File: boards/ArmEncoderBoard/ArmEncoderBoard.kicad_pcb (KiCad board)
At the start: 2 copper layers, 34 x 42.5 mm, 5 parts, among them J1 S6B-PH-SM4-TB

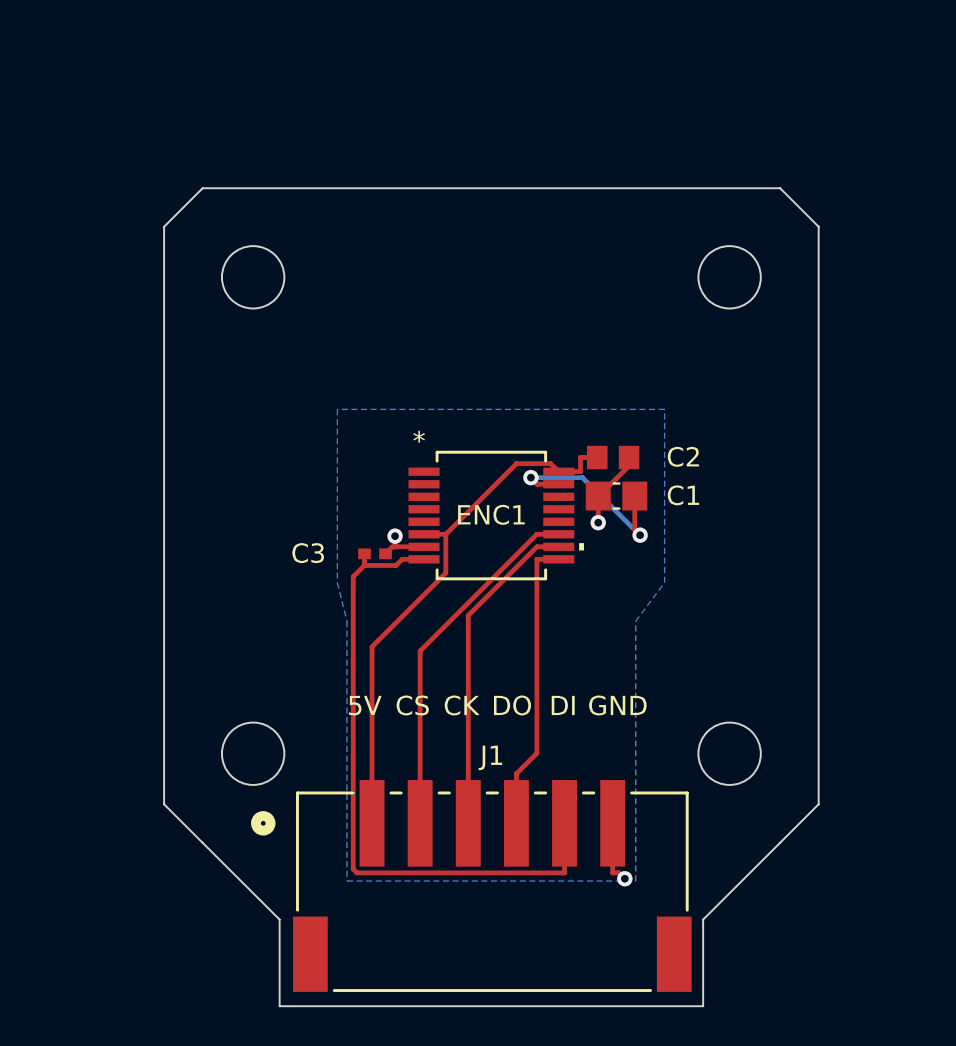
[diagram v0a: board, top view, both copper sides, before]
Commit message: Split into leg and arm, finish arm encoder
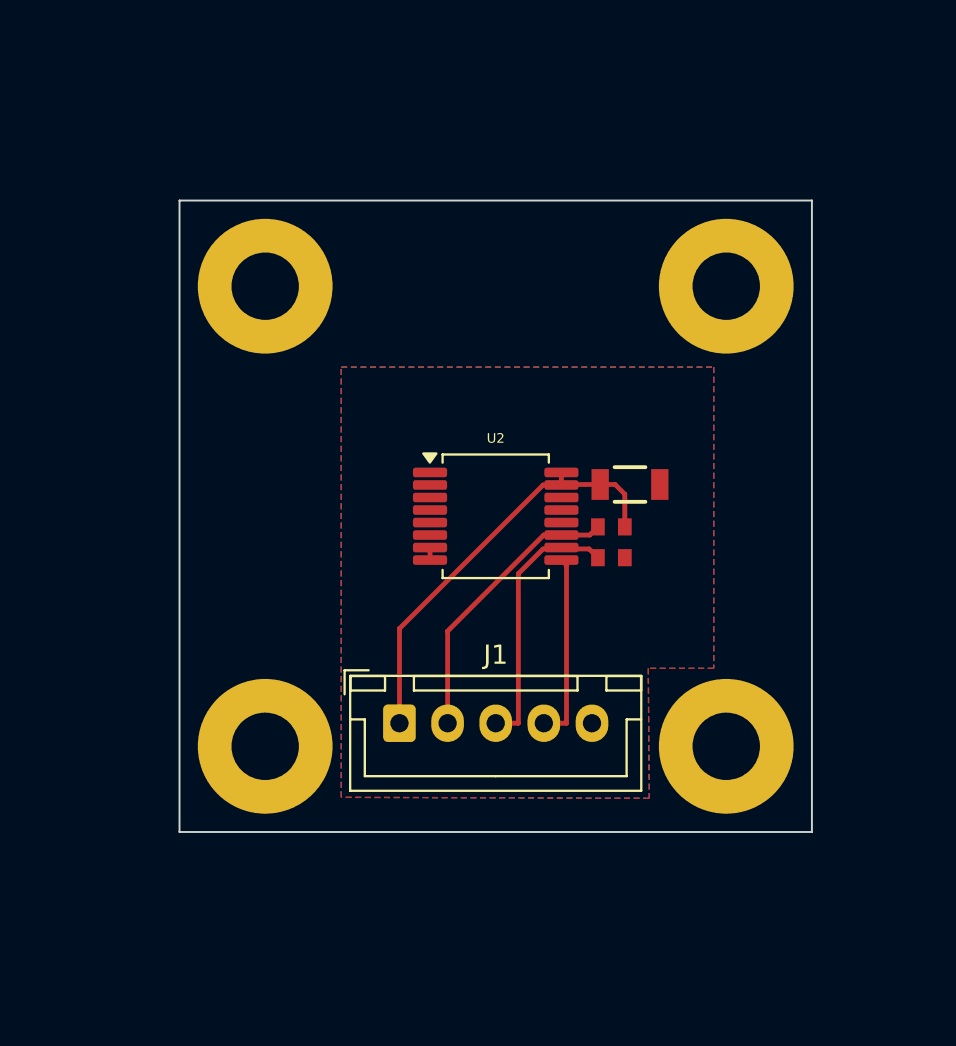
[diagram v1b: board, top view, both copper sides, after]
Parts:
- removed C2: CC0805KRX7R7BB104, AS5045-DECOP-CAP:CC0805N_YAG
- removed C3: CC0402KRX7R7BB104, AS5045-PROG-CAP:YAG_CC0402_YAG
- removed ENC1: AS5045-ASST, AS5045:SSOP16_AS5040-ASST_AMS
- added H1: MountingHole, MountingHole:MountingHole_3.5mm_Pad, F.Cu at (126.8, 70.1)
- added H2: MountingHole, MountingHole:MountingHole_3.5mm_Pad, F.Cu at (150.7, 70.1)
- added H3: MountingHole, MountingHole:MountingHole_3.5mm_Pad, F.Cu at (126.8, 94.0)
- added H4: MountingHole, MountingHole:MountingHole_3.5mm_Pad, F.Cu at (150.7, 94.0)
- added R1: 4.7K, Resistor4.7K:CR0603-FX-4701ELF, F.Cu at (144.7, 84.2)
- added R2: 4.7K, Resistor4.7K:CR0603-FX-4701ELF, F.Cu at (144.7, 82.6)
- added U2: AS5045B, Package_SO:SSOP-16_5.3x6.2mm_P0.65mm, F.Cu at (138.7, 82.0)
- C1: value CC0805KKX5R7BB106 -> 100nF; footprint AS5045-3V3-REG-CAP:CAPC2012X70 -> Capacitor100nF:885342208002
- J1: value S6B-PH-SM4-TB -> Conn_01x05; footprint JST-XH-6:CONN_S6B-XH-SM4-TB_JST -> Connector_JST:JST_XH_B5B-XH-A_1x05_P2.50mm_Vertical
- moved J1 10.00 mm to (133.7, 92.8)
- moved C1 0.92 mm to (145.7, 80.4), turned to 180 degrees
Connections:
- C1 pad 2: Net-(ENC1-VDD3V3) -> VIN
- J1 pad 1: +5V -> VIN
- J1 pad 2: Net-(ENC1-CSN) -> CS
- J1 pad 3: Net-(ENC1-CLK) -> SCK
- J1 pad 4: Net-(ENC1-DO) -> MISO
- J1 pad 5: Net-(ENC1-PROG) -> GND
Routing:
- net Net-(ENC1-PROG): track 33.5 -> 0.00 mm
- net +5V: track 28.0 -> 0.00 mm
- net VIN: track 0.00 -> 22.3 mm
- net Net-(ENC1-CSN): track 18.7 -> 0.00 mm
- net Net-(ENC1-CLK): track 17.0 -> 0.00 mm
- net Net-(ENC1-DO): track 15.3 -> 0.00 mm
- net CS: track 0.00 -> 14.8 mm
- net SCK: track 0.00 -> 13.9 mm
- net Net-(ENC1-VDD3V3): track 10.7 -> 0.00 mm, vias 2 -> 0
- net MISO: track 0.00 -> 9.76 mm
- net GND: track 10.1 -> 0.65 mm, vias 3 -> 0
- added copper zone on F.Cu, net GND
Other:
- board size 34 x 42.5 mm -> 32.9 x 32.8 mm
- board text removed: "5V"
- board text removed: "CK"
- board text removed: "CS"
- board text removed: "DI"
- board text removed: "DO"
- board text removed: "GND"

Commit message: Leg encoder board pre-final
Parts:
- moved J1 2.00 mm to (133.7, 90.8)
- moved H2 0.58 mm to (151.1, 69.7)
- moved H4 0.58 mm to (151.1, 94.4)
- moved H1 0.58 mm to (126.4, 69.7)
- moved H3 0.58 mm to (126.4, 94.4)
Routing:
- net MISO: track 9.76 -> 13.8 mm
- net SCK: track 13.9 -> 10.9 mm
- net VIN: track 22.3 -> 20.3 mm
- net CS: track 14.8 -> 12.8 mm
- net GND: track 0.65 -> 0.00 mm
- removed copper zone on B.Cu, net GND
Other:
- board size 32.9 x 32.8 mm -> 34 x 34 mm
- board text added: "3V3"
- board text added: "CS"
- board text added: "GND"
- board text added: "MISO"
- board text added: "SCK"
- board text added: "SSI"

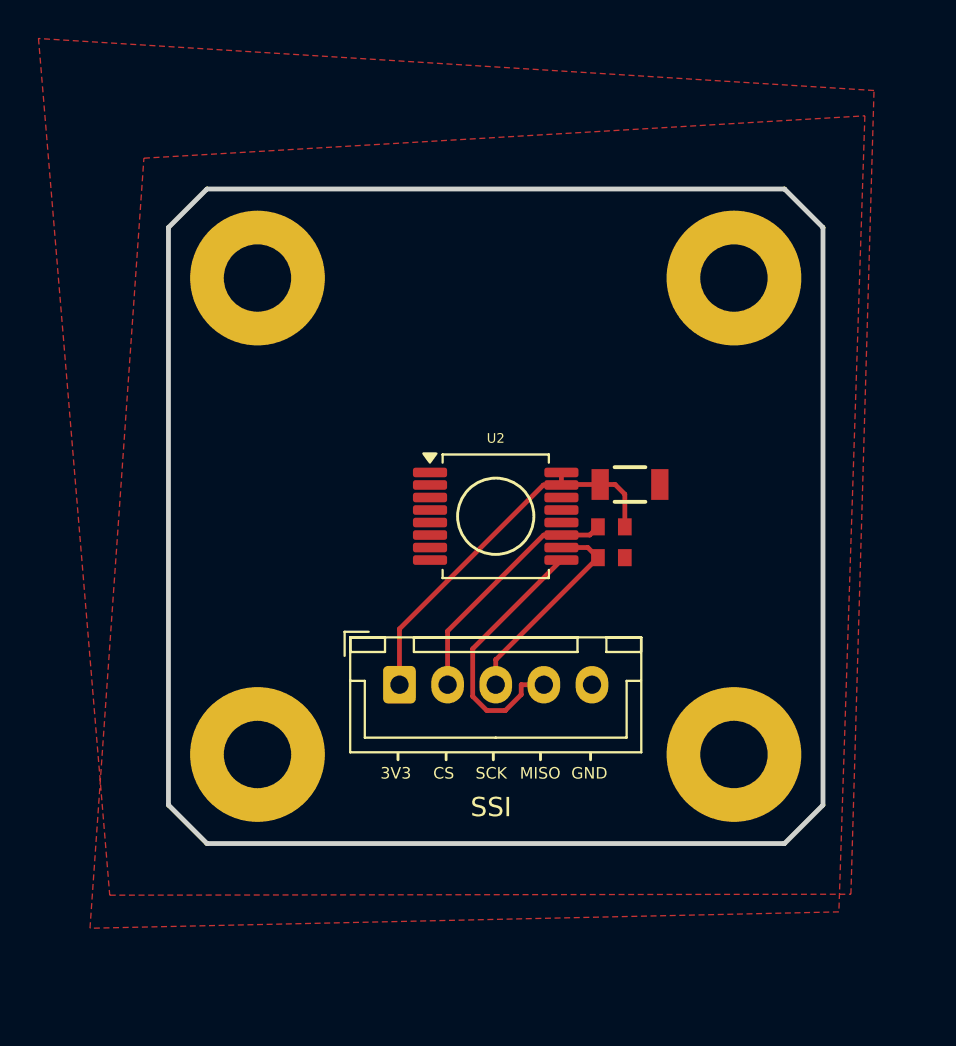
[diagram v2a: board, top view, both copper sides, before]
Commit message: Arm encoder initial bom update
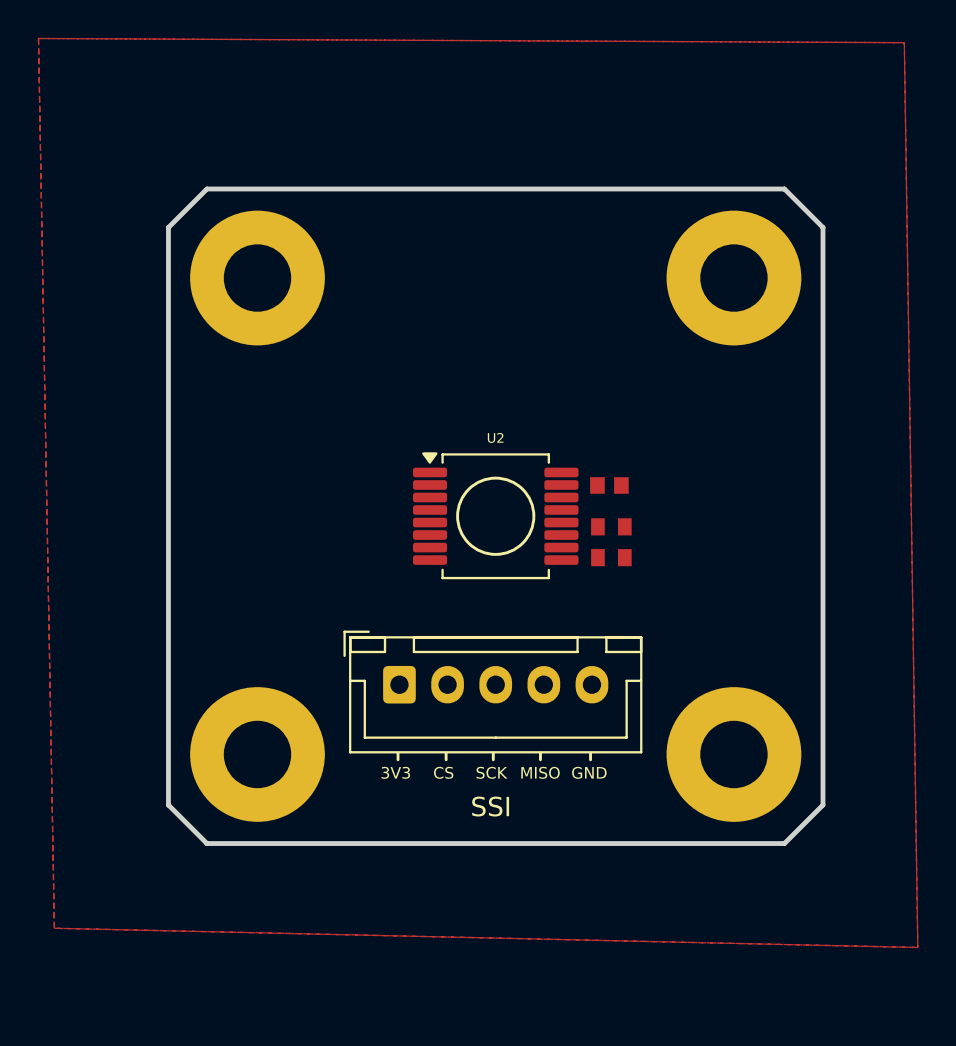
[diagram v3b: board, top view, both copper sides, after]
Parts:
- C1: footprint Capacitor100nF:885342208002 -> Capacitor100nF:CC0603KRX7R9BB104
- moved C1 1.07 mm to (144.6, 80.5)
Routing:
- net VIN: track 20.3 -> 0.00 mm
- net MISO: track 13.8 -> 0.00 mm
- net CS: track 12.8 -> 0.00 mm
- net SCK: track 10.9 -> 0.00 mm

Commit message: Prepare encoder boards for manufacturing
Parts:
- added C2: 0.1uF, Capacitor100nF:CC0603KRX7R9BB104, F.Cu at (132.2, 82.2)
- added C3: 1uF, Capacitor1uF:CC0603JRX7R7BB105-L, F.Cu at (137.3, 73.3)
- added C4: 1uF, Capacitor1uF:CC0603JRX7R7BB105-L, F.Cu at (140.7, 73.3)
- added CR1: BAT54, EnvelopeDiode:BAT54WS-7-F, F.Cu at (133.6, 77.0)
- added CR2: BAT54, EnvelopeDiode:BAT54WS-7-F, F.Cu at (144.3, 77.0)
- added D1: LEDBLUE, LedBlue:YLED0603B, F.Cu at (129.1, 82.2)
- added D2: LEDRED, LedRed:YLED0603R, F.Cu at (148.2, 82.2)
- added Q1: SS8050, Package_TO_SOT_SMD:SOT-23, F.Cu at (133.7, 71.4)
- added Q2: SS8050, Package_TO_SOT_SMD:SOT-23, F.Cu at (144.2, 71.4)
- added R3: 150R, Resistor150:RESC1607X60N, F.Cu at (125.9, 82.3)
- added R4: 1K, Resistor1K:RCG06031K00FKEA, F.Cu at (151.3, 82.3)
- added R5: 47K, Resistor47K:RC0603FR-0747KL, F.Cu at (130.9, 75.2)
- added R6: 100K, Resistor100K:CRCW0603100KFKEA, F.Cu at (137.3, 70.5)
- added R7: 100K, Resistor100K:CRCW0603100KFKEA, F.Cu at (140.6, 70.5)
- added R8: 47K, Resistor47K:RC0603FR-0747KL, F.Cu at (146.8, 75.2)
- added U1: DBV6, SchmittBuffer:SN74LVC2G17DBVR, F.Cu at (138.9, 76.3)
- moved J1 2.40 mm to (133.8, 93.2)
- moved R2 0.41 mm to (144.8, 82.2)
- moved C1 0.12 mm to (144.8, 80.5)
- moved R1 0.07 mm to (144.8, 84.2)
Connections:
- U2 pad 3: unconnected-(U2-A-Pad3) -> A
- U2 pad 6: unconnected-(U2-I-Pad6) -> I
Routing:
- net VIN: track 0.00 -> 47.7 mm
- net GND: track 0.00 -> 23.7 mm, vias 0 -> 4
- net SCK: track 0.00 -> 17.1 mm
- net CS: track 0.00 -> 15.7 mm
- net /BLUE_CATHODE: track 0.00 -> 14.2 mm
- net /RED_CATHODE: track 0.00 -> 13.8 mm
- net /I_ENV: track 0.00 -> 11.4 mm
- net /A_ENV: track 0.00 -> 11.4 mm
- net MISO: track 0.00 -> 9.22 mm
- net A: track 0.00 -> 8.64 mm
- net A_BUF: track 0.00 -> 8.13 mm
- net I: track 0.00 -> 7.65 mm
- net I_BUF: track 0.00 -> 4.55 mm
- net Net-(Q2-B): track 0.00 -> 4.39 mm
- net /RED_ANODE: track 0.00 -> 4.25 mm
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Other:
- board text removed: "SSI"
